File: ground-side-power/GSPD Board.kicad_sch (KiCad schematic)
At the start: 41 parts, among them J1 Battery Terminals, J2 Battery Terminals, J3 Battery Terminals, J4 Battery Terminals, J5 455860005, J6 455860005, J7 ATX-24, K1 AZ2150-1A-12DEF, SW1 SW_SP3T, U1 K7805-3AR3, U2 URB2424LD-20WR3

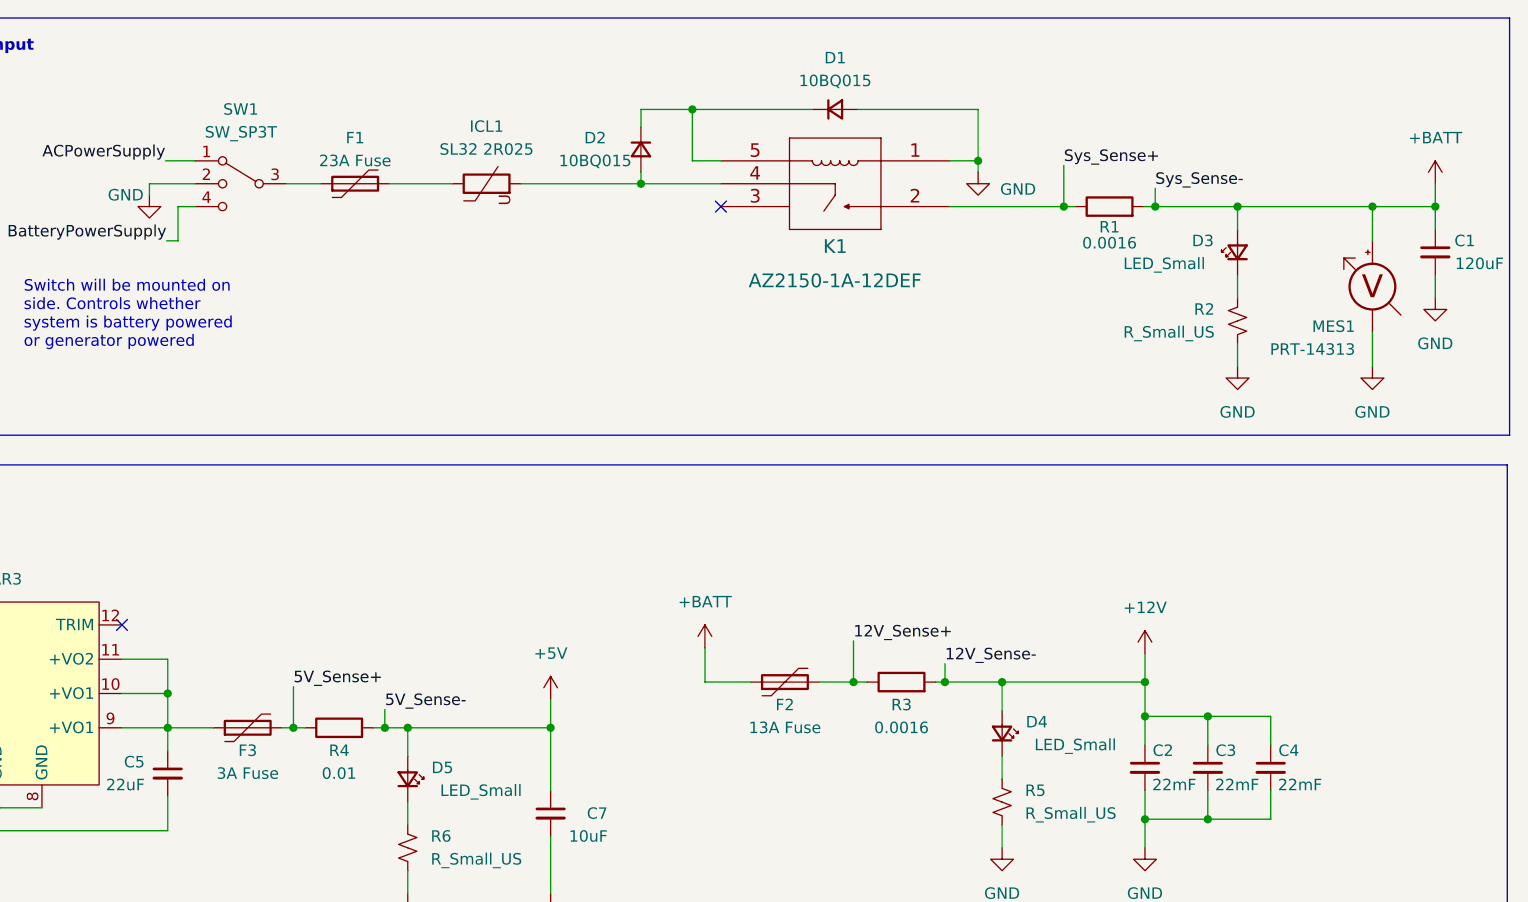
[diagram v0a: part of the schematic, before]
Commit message: Added Footprints
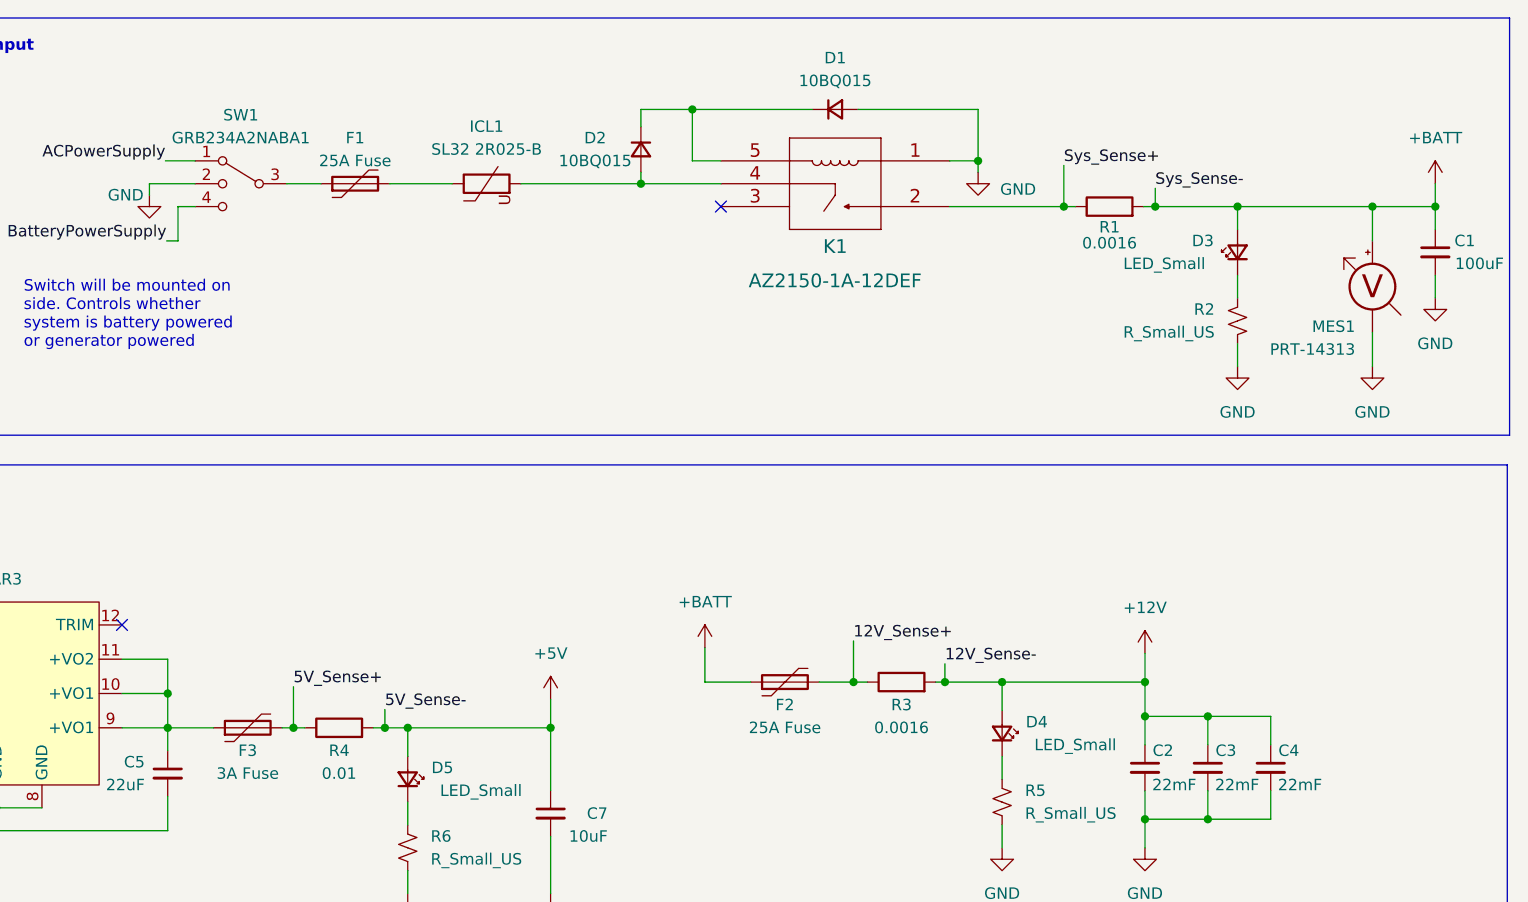
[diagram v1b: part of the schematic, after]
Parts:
- C1: value 120uF -> 100uF; footprint (none) -> Capacitor_SMD:C_1206_3216Metric_Pad1.33x1.80mm_HandSolder
- C10, C5, C6, C7, D1: footprint (none) -> Capacitor_SMD:C_0603_1608Metric_Pad1.08x0.95mm_HandSolder
- C2, C3, C4: footprint (none) -> GSP:LLS1C223MELZ
- C8, C9: footprint (none) -> Capacitor_SMD:C_1206_3216Metric_Pad1.33x1.80mm_HandSolder
- D2: footprint (none) -> Diode_SMD:D_SMB
- D3, D4, D5, D6: footprint (none) -> Diode_SMD:D_0805_2012Metric
- F1: value 23A Fuse -> 25A Fuse; footprint (none) -> Fuse:Fuse_1206_3216Metric_Pad1.42x1.75mm_HandSolder
- F2: value 13A Fuse -> 25A Fuse; footprint (none) -> Fuse:Fuse_1206_3216Metric_Pad1.42x1.75mm_HandSolder
- F3, F4: footprint (none) -> Fuse:Fuse_1206_3216Metric_Pad1.42x1.75mm_HandSolder
- ICL1: value SL32 2R025 -> SL32 2R025-B; footprint (none) -> GSP:SL32 2R025-B
- J1, J2, J3, J4, MES1: footprint (none) -> GSP:OSTTA020161
- J5, J6: footprint CON_455860005_MOL -> GSP:MOLEX_455860005
- J7: footprint (none) -> GSP:MOLEX_15246240
- K1: footprint (none) -> GSP:AZ2150-1A-12DEF
- R2, R5, R6, R8: footprint (none) -> Resistor_SMD:R_1020_2550Metric_Pad1.33x5.20mm_HandSolder
- SW1: value SW_SP3T -> GRB234A2NABA1; footprint (none) -> Resistor_SMD:R_1020_2550Metric_Pad1.33x5.20mm_HandSolder
- U1: footprint (none) -> GSP:K7805-3AR3
- U2: footprint (none) -> GSP:URB2424LD-20WR3

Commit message: Fixed footprints
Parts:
- removed SW1: GRB234A2NABA1, Resistor_SMD:R_1020_2550Metric_Pad1.33x5.20mm_HandSolder, symbol Switch:SW_SP3T
- added SW1: GRB234A2NABA1, GSP:TB005-762-03BE, symbol Switch:SW_SPDT
- R1, R3, R4, R7: footprint Resistor_SMD:R_1206_3216Metric_Pad1.42x1.75mm_HandSolder -> Resistor_SMD:R_1206_3216Metric_Pad1.30x1.75mm_HandSolder
- R2, R5, R6, R8: footprint Resistor_SMD:R_1020_2550Metric_Pad1.33x5.20mm_HandSolder -> Resistor_SMD:R_1206_3216Metric_Pad1.30x1.75mm_HandSolder
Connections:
- net ACPowerSupply: now also SW1.1 (A)
- net BatteryPowerSupply: now also SW1.3 (C)
- net at F1.1: now also SW1.2 (B)
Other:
- note added: "Physical switch has 3 positions. 3rd position is nc from circuit."

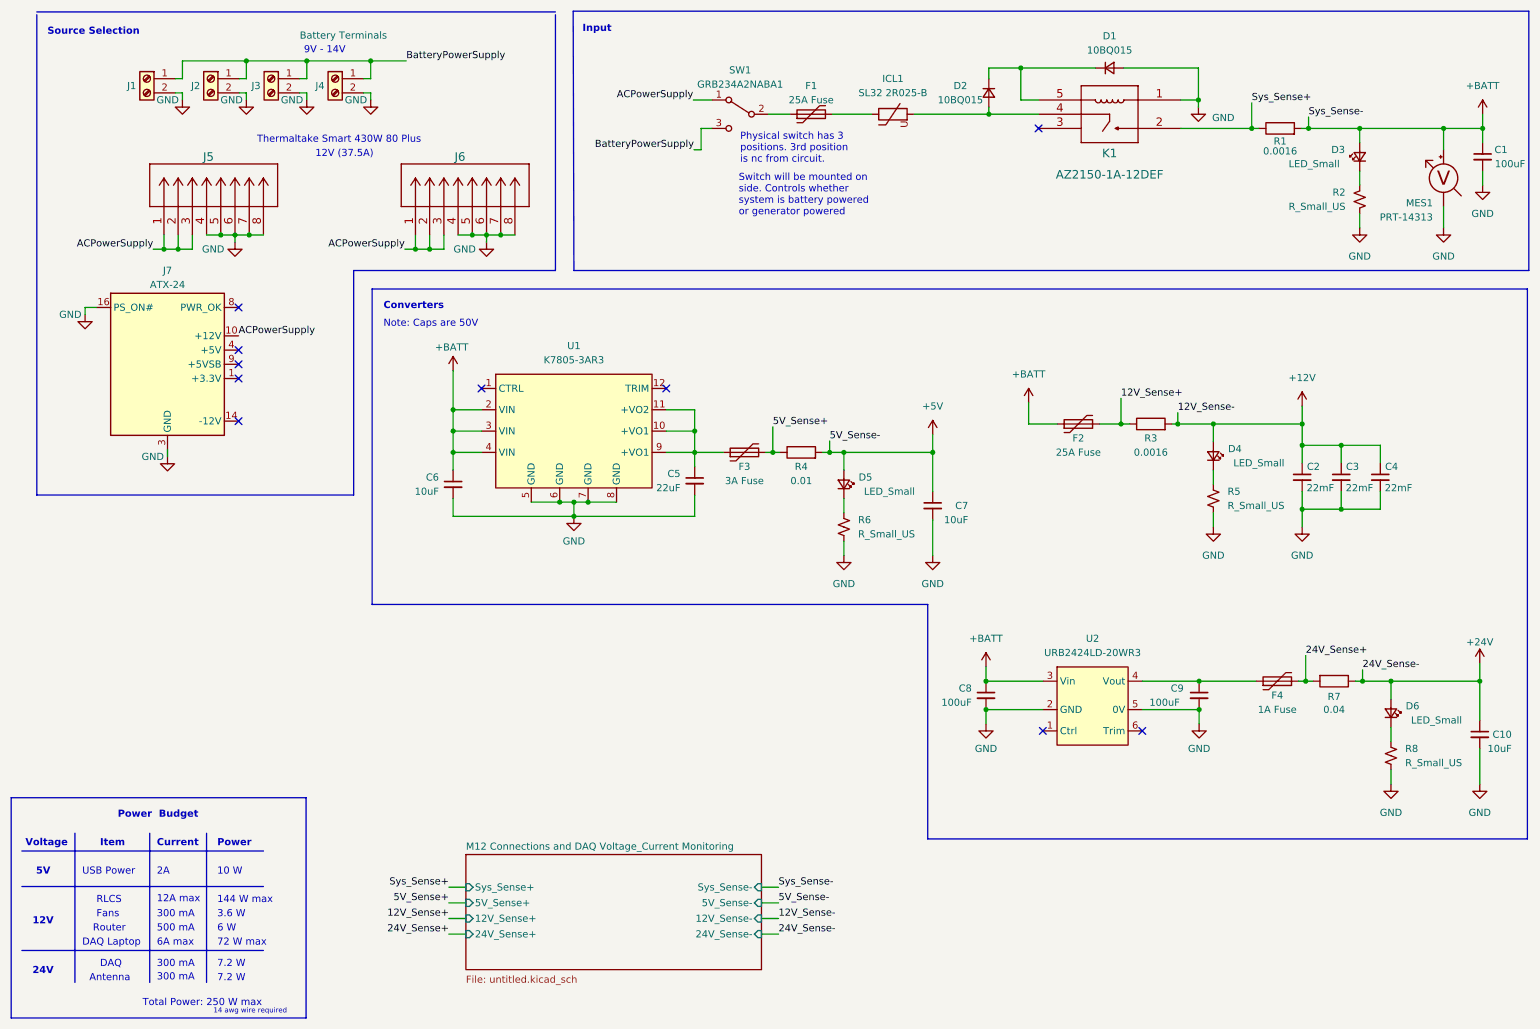
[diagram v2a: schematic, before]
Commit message: Split into multiple boards
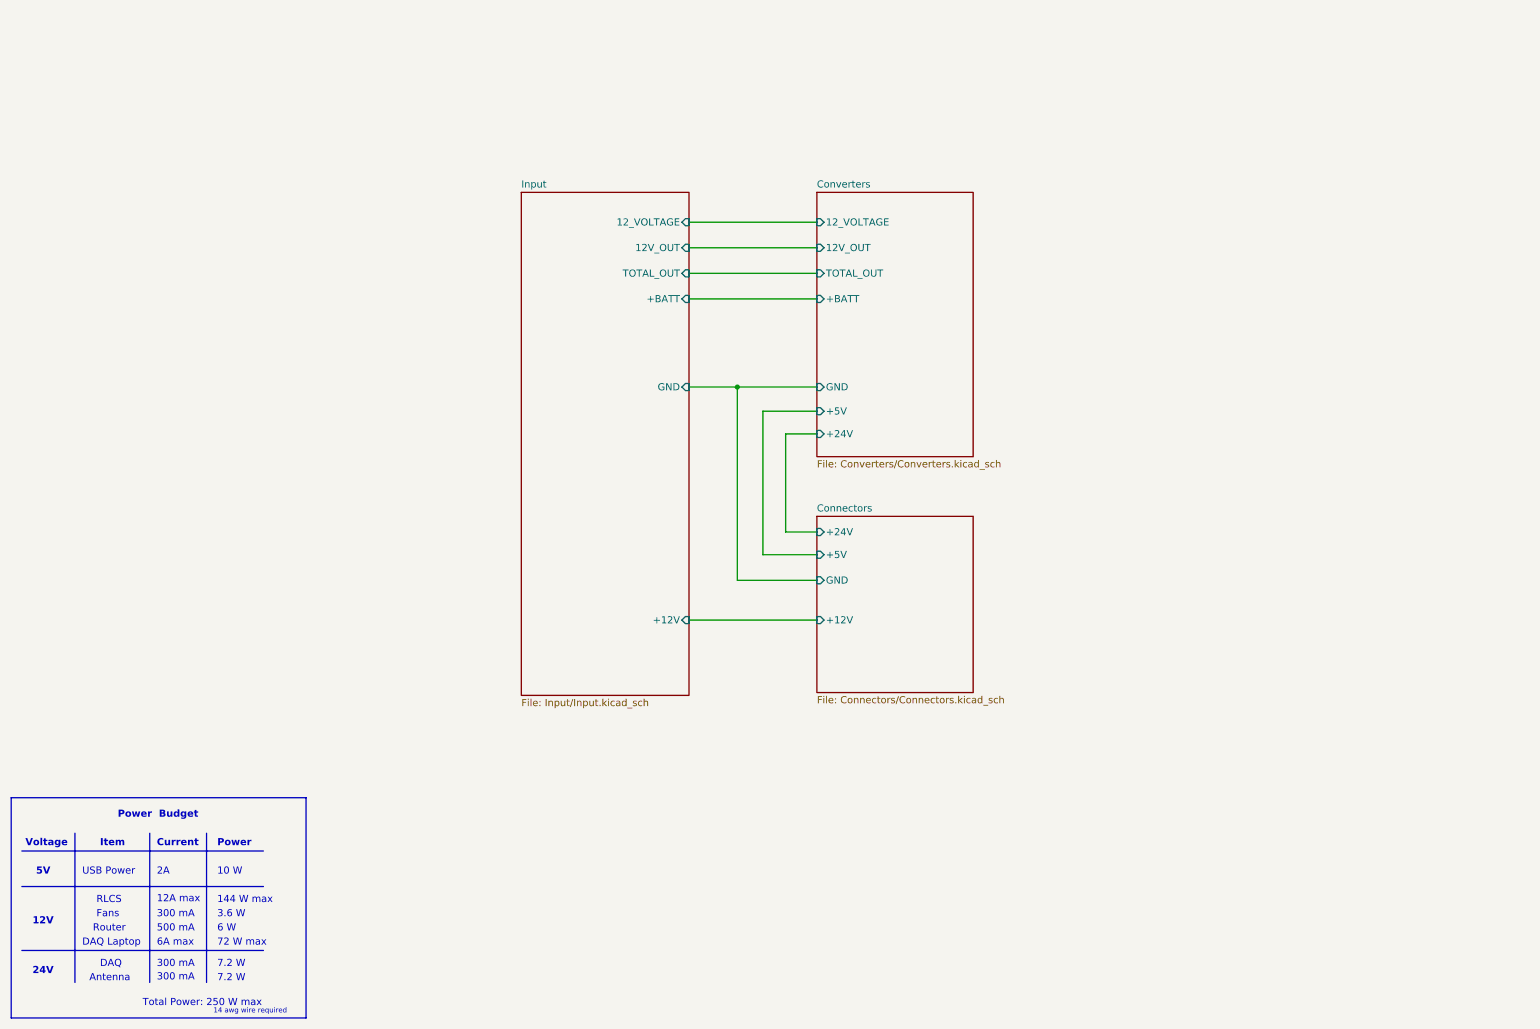
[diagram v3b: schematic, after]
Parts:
- removed C1, C8, C9: 100uF, Capacitor_SMD:C_1206_3216Metric_Pad1.33x1.80mm_HandSolder, symbol Device:C_Small
- removed C10, C6, C7: 10uF, Capacitor_SMD:C_0603_1608Metric_Pad1.08x0.95mm_HandSolder, symbol Device:C_Small
- removed C2, C3, C4: 22mF, GSP:LLS1C223MELZ, symbol Device:C_Small
- removed C5: 22uF, Capacitor_SMD:C_0603_1608Metric_Pad1.08x0.95mm_HandSolder, symbol Device:C_Small
- removed D1: 10BQ015, Capacitor_SMD:C_0603_1608Metric_Pad1.08x0.95mm_HandSolder, symbol Device:D_Small
- removed D2: 10BQ015, Diode_SMD:D_SMB, symbol Device:D_Small
- removed D3, D4, D5, D6: LED_Small, Diode_SMD:D_0805_2012Metric, symbol Device:LED_Small
- removed F1, F2: 25A Fuse, Fuse:Fuse_1206_3216Metric_Pad1.42x1.75mm_HandSolder, symbol Device:Polyfuse
- removed F3: 3A Fuse, Fuse:Fuse_1206_3216Metric_Pad1.42x1.75mm_HandSolder, symbol Device:Polyfuse
- removed F4: 1A Fuse, Fuse:Fuse_1206_3216Metric_Pad1.42x1.75mm_HandSolder, symbol Device:Polyfuse
- removed ICL1: SL32 2R025-B, GSP:SL32 2R025-B, symbol Device:Varistor
- removed J1, J2, J3, J4: Battery Terminals, GSP:OSTTA020161, symbol Connector:Screw_Terminal_01x02
- removed J5, J6: 455860005, GSP:MOLEX_455860005, symbol GSP:455860005
- removed J7: ATX-24, GSP:MOLEX_15246240, symbol Connector:ATX-24
- removed K1: AZ2150-1A-12DEF, GSP:AZ2150-1A-12DEF, symbol GSP:AZ2150-1A-12DEF
- removed MES1: PRT-14313, GSP:OSTTA020161, symbol Device:Voltmeter_DC
- removed R1, R3: 0.0016, Resistor_SMD:R_1206_3216Metric_Pad1.30x1.75mm_HandSolder, symbol Device:R
- removed R2, R5, R6, R8: R_Small_US, Resistor_SMD:R_1206_3216Metric_Pad1.30x1.75mm_HandSolder, symbol Device:R_Small_US
- removed R4: 0.01, Resistor_SMD:R_1206_3216Metric_Pad1.30x1.75mm_HandSolder, symbol Device:R
- removed R7: 0.04, Resistor_SMD:R_1206_3216Metric_Pad1.30x1.75mm_HandSolder, symbol Device:R
- removed SW1: GRB234A2NABA1, GSP:TB005-762-03BE, symbol Switch:SW_SPDT
- removed U1: K7805-3AR3, GSP:K7805-3AR3, symbol Regulator_Switching:AP63203WU
- removed U2: URB2424LD-20WR3, GSP:URB2424LD-20WR3, symbol GSP:URB2424LD-30WR3
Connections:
- no-connect marks 10 -> 0
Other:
- removed sheet M12 Connections and DAQ Voltage_Current Monitoring
- added sheet Connectors (Connectors/Connectors.kicad_sch)
- added sheet Converters (Converters/Converters.kicad_sch)
- added sheet Input (Input/Input.kicad_sch)
- note removed: "12V (37.5A)"
- note removed: "9V - 14V"
- note removed: "Converters"
- note removed: "Input"
- note removed: "Note: Caps are 50V"
- note removed: "Physical switch has 3 positions. 3rd position is nc from circuit."
- note removed: "Source Selection"
- note removed: "Switch will be mounted on side. Controls whether system is battery powered or generator powered"
- note removed: "Thermaltake Smart 430W 80 Plus"
